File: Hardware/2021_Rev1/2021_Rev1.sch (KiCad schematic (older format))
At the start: 37 parts

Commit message: Schematic almost finished
Switches, Joystick connector, Analog gauge
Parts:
- added Conn1: Joystick_OUT, symbol MRDT_Connectors:Molex_SL_04
- added Conn2: Joystick_GND, symbol MRDT_Connectors:Molex_SL_04
- added Conn3: ELEV, symbol MRDT_Connectors:Molex_SL_02
- added Conn4: AZI, symbol MRDT_Connectors:Molex_SL_02
- added Conn5: Switches, symbol MRDT_Connectors:Molex_SL_10
- added Conn6: Green_LED, symbol MRDT_Connectors:Molex_SL_02
- added J?: Conn_01x18_Shielded, symbol Connector_Generic_Shielded:Conn_01x18_Shielded
- U2: renamed from U?; value LM2576D2TR4 -> LM2576SX-3.3
- U3: renamed from U?; value LM2576D2TR4 -> LM2576SX-5.0
- gave numbers to parts that had none: 28
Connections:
- wire segments 134 -> 237
- no-connect marks 5 -> 71

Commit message: Schematic almost finished
added LCD display
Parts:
- removed J?: Conn_01x18_Shielded, symbol Connector_Generic_Shielded:Conn_01x18_Shielded
- added 4.7K (x2): R, symbol Device:R
- added U?: PCF8574, symbol Interface_Expansion:PCF8574
- added U?: RC1602A, Display:RC1602A, symbol Display_Character:RC1602A
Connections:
- net labels added: P3, SCL, SDA, VO, k
- wire segments 237 -> 283
- no-connect marks 71 -> 76
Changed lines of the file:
@@
 U 1 1 5FABE786
 P 7000 4500
-F 0 "Conn6" H 7128 4658 60  0000 L CNN
-F 1 "Green_LED" H 7128 4552 60  0000 L CNN
+F 0 "Conn6" H 6900 4350 60  0000 L CNN
+F 1 "Green_LED" H 6850 4450 60  0000 L CNN
 F 2 "" H 7000 4400 60  0001 C CNN
 F 3 "" H 7000 4400 60  0001 C CNN
@@
 	5350 4400 5150 4400
 $Comp
-L Connector_Generic_Shielded:Conn_01x18_Shielded J?
-U 1 1 60174413
-P 10300 3750
-F 0 "J?" H 10388 3663 50  0000 L CNN
-F 1 "Conn_01x18_Shielded" H 10388 3572 50  0000 L CNN
-F 2 "" H 10300 3750 50  0001 C CNN
-F 3 "~" H 10300 3750 50  0001 C CNN
-	1    10300 3750
-	1    0    0    -1
-$EndComp
+L Display_Character:RC1602A U?
+U 1 1 5FA70A2A
+P 9650 5500
+F 0 "U?" H 9800 6300 50  0000 C CNN
+F 1 "RC1602A" H 9900 6200 50  0000 C CNN
+F 2 "Display:RC1602A" H 9750 4700 50  0001 C CNN
+F 3 "http://www.raystar-optronics.com/down.php?ProID=18" H 9750 5400 50  0001 C CNN
+	1    9650 5500
+	1    0    0    -1
+$EndComp
+Wire Wire Line
+	8950 5000 9250 5000
+Wire Wire Line
+	8950 5100 9250 5100
+Wire Wire Line
+	8950 5200 9250 5200
+Wire Wire Line
+	8950 5700 9000 5700
+Wire Wire Line
+	9000 5700 9000 6000
+Wire Wire Line
+	9000 6000 9250 6000
+Wire Wire Line
+	8950 5600 9050 5600
+Wire Wire Line
+	9050 5600 9050 5900
+Wire Wire Line
+	9050 5900 9250 5900
+Wire Wire Line
+	8950 5500 9100 5500
+Wire Wire Line
+	9100 5500 9100 5800
+Wire Wire Line
+	9100 5800 9250 5800
+Wire Wire Line
+	8950 5400 9150 5400
+Wire Wire Line
+	9150 5400 9150 5700
+Wire Wire Line
+	9150 5700 9250 5700
+NoConn ~ 9200 5300
+NoConn ~ 9200 5400
+NoConn ~ 9200 5500
+NoConn ~ 9200 5600
+Wire Wire Line
+	9200 5300 9250 5300
+Wire Wire Line
+	9200 5400 9250 5400
+Wire Wire Line
+	9200 5500 9250 5500
+Wire Wire Line
+	9200 5600 9250 5600
+$Comp
+L power:GND #PWR?
+U 1 1 5FBB576D
+P 9650 6300
+F 0 "#PWR?" H 9650 6050 50  0001 C CNN
+F 1 "GND" H 9655 6127 50  0000 C CNN
+F 2 "" H 9650 6300 50  0001 C CNN
+F 3 "" H 9650 6300 50  0001 C CNN
+	1    9650 6300
+	1    0    0    -1
+$EndComp
+$Comp
+L power:GND #PWR?
+U 1 1 5FBB5B62
+P 8450 6200
+F 0 "#PWR?" H 8450 5950 50  0001 C CNN
+F 1 "GND" H 8455 6027 50  0000 C CNN
+F 2 "" H 8450 6200 50  0001 C CNN
+F 3 "" H 8450 6200 50  0001 C CNN
+	1    8450 6200
+	1    0    0    -1
+$EndComp
+$Comp
+L power:GND #PWR?
+U 1 1 5FBB69D1
+P 7750 5900
+F 0 "#PWR?" H 7750 5650 50  0001 C CNN
+F 1 "GND" H 7755 5727 50  0000 C CNN
+F 2 "" H 7750 5900 50  0001 C CNN
+F 3 "" H 7750 5900 50  0001 C CNN
+	1    7750 5900
+	1    0    0    -1
+$EndComp
+NoConn ~ 7850 5800
+Wire Wire Line
+	8450 6100 8450 6200
+Wire Wire Line
+	9650 6200 9650 6300
+Wire Wire Line
+	7850 5800 7950 5800
+Wire Wire Line
+	7750 5900 7750 5500
+Wire Wire Line
+	7750 5300 7950 5300
+Wire Wire Line
+	7950 5400 7750 5400
+Connection ~ 7750 5400
+Wire Wire Line
+	7750 5400 7750 5300
+Wire Wire Line
+	7950 5500 7750 5500
+Connection ~ 7750 5500
+Wire Wire Line
+	7750 5500 7750 5400
+Text GLabel 9000 5300 2    50   Output ~ 0
+P3
+Wire Wire Line
+	8950 5300 9000 5300
+Text GLabel 10150 5300 2    50   Output ~ 0
+VO
+$Comp
+L power:+5V #PWR?
+U 1 1 5FC8AC31
+P 10600 5800
+F 0 "#PWR?" H 10600 5650 50  0001 C CNN
+F 1 "+5V" H 10615 5973 50  0000 C CNN
+F 2 "" H 10600 5800 50  0001 C CNN
+F 3 "" H 10600 5800 50  0001 C CNN
+	1    10600 5800
+	1    0    0    -1
+$EndComp
+Text GLabel 10150 5700 2    50   Output ~ 0
+k
+Text GLabel 7550 5000 0    50   Output ~ 0
+SCL
+Text GLabel 7550 5100 0    50   Output ~ 0
+SDA
+$Comp
+L power:+5V #PWR?
+U 1 1 5FC8EC9F
+P 7450 4600
+F 0 "#PWR?" H 7450 4450 50  0001 C CNN
+F 1 "+5V" H 7465 4773 50  0000 C CNN
+F 2 "" H 7450 4600 50  0001 C CNN
+F 3 "" H 7450 4600 50  0001 C CNN
+	1    7450 4600
+	1    0    0    -1
+$EndComp
+$Comp
+L Device:R 4.7K
+U 1 1 5FCAFDA1
+P 7650 4800
+F 0 "4.7K" V 7650 4700 50  0000 L CNN
+F 1 "R" H 7720 4755 50  0000 L CNN
+F 2 "" V 7580 4800 50  0001 C CNN
+F 3 "~" H 7650 4800 50  0001 C CNN
+	1    7650 4800
+	1    0    0    -1
+$EndComp
+$Comp
+L Device:R 4.7K
+U 1 1 5FCB0E54
+P 7850 4800
+F 0 "4.7K" V 7850 4700 50  0000 L CNN
+F 1 "R" H 7920 4755 50  0000 L CNN
+F 2 "" V 7780 4800 50  0001 C CNN
+F 3 "~" H 7850 4800 50  0001 C CNN
+	1    7850 4800
+	1    0    0    -1
+$EndComp
+$Comp
+L Interface_Expansion:PCF8574 U?
+U 1 1 5FA6EB0D
+P 8450 5400
+F 0 "U?" H 8600 6200 50  0000 C CNN
+F 1 "PCF8574" H 8700 6100 50  0000 C CNN
+F 2 "" H 8450 5400 50  0001 C CNN
+F 3 "http://www.nxp.com/documents/data_sheet/PCF8574_PCF8574A.pdf" H 8450 5400 50  0001 C CNN
+	1    8450 5400
+	1    0    0    -1
+$EndComp
+Wire Wire Line
+	7550 5000 7850 5000
+Wire Wire Line
+	7550 5100 7650 5100
+Wire Wire Line
+	7650 4950 7650 5100
+Connection ~ 7650 5100
+Wire Wire Line
+	7650 5100 7950 5100
+Wire Wire Line
+	7850 4950 7850 5000
+Connection ~ 7850 5000
+Wire Wire Line
+	7850 5000 7950 5000
+Wire Wire Line
+	7450 4600 7650 4600
+Wire Wire Line
+	8450 4600 8450 4700
+Wire Wire Line
+	8450 4600 9650 4600
+Wire Wire Line
+	9650 4600 9650 4800
+Connection ~ 8450 4600
+Wire Wire Line
+	7850 4650 7850 4600
+Connection ~ 7850 4600
+Wire Wire Line
+	7850 4600 8450 4600
+Wire Wire Line
+	7650 4650 7650 4600
+Connection ~ 7650 4600
+Wire Wire Line
+	7650 4600 7850 4600
+Wire Wire Line
+	10050 5300 10150 5300
+Wire Wire Line
+	10050 5700 10150 5700
+Wire Wire Line
+	10050 5800 10600 5800
 $EndSCHEMATC

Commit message: Layout Started
Bucks and LCD circuit replaced with OKIs and spark fun LCD
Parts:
- removed 4.7K (x2): R, symbol Device:R
- removed D1, D3: D_Schottky, symbol Device:D_Schottky
- removed D2, D4: GREEN, symbol Device:LED
- removed L1, L2: 100uH, symbol Device:L_Small
- removed R1: 330, symbol Device:R
- removed R2: 500, symbol Device:R
- removed TP1, TP2: TestPoint, symbol Connector:TestPoint
- removed U2: LM2576SX-3.3, symbol MRDT_Devices:LM2576D2TR4
- removed U3: LM2576SX-5.0, symbol MRDT_Devices:LM2576D2TR4
- removed U?: PCF8574, symbol Interface_Expansion:PCF8574
- removed U?: RC1602A, Display:RC1602A, symbol Display_Character:RC1602A
- added BT1: BC9VPC, Packages:BAT_BC9VPC, symbol BC9VPC:BC9VPC
- added Conn8: Molex_SL_03, MRDT_Connectors:MOLEX_SL_03_Vertical, symbol MRDT_Connectors:Molex_SL_03
- added U2, U3: OKI, MRDT_Devices:OKI_Horizontal, symbol MRDT_Devices:OKI
- C1, C3: value 100uF -> 10uF; footprint (none) -> Capacitor_SMD:C_0603_1608Metric_Pad1.08x0.95mm_HandSolder
- C2, C4: value 1000uF -> 10uF; footprint (none) -> Capacitor_SMD:C_0603_1608Metric_Pad1.08x0.95mm_HandSolder
- C5, C6, C7: footprint (none) -> Capacitor_SMD:C_0603_1608Metric_Pad1.08x0.95mm_HandSolder
- Conn2: renamed from Conn1; footprint (none) -> MRDT_Connectors:MOLEX_SL_04_Vertical
- Conn3: renamed from Conn2; footprint (none) -> MRDT_Connectors:MOLEX_SL_04_Vertical
- Conn4: renamed from Conn3; footprint (none) -> MRDT_Connectors:MOLEX_SL_02_Vertical
- Conn5: renamed from Conn4; footprint (none) -> MRDT_Connectors:MOLEX_SL_02_Vertical
- Conn6: renamed from Conn5; footprint (none) -> MRDT_Connectors:MOLEX_SL_10_Vertical
- Conn7: renamed from Conn6; footprint (none) -> MRDT_Connectors:MOLEX_SL_02_Vertical
- D1: renamed from D5; footprint (none) -> LED_SMD:LED_0603_1608Metric_Pad1.05x0.95mm_HandSolder
- D2: renamed from D6; footprint (none) -> LED_SMD:LED_0603_1608Metric_Pad1.05x0.95mm_HandSolder
- J1: footprint (none) -> Connector_USB:USB_A_Stewart_SS-52100-001_Horizontal
- R1: renamed from R3; footprint (none) -> Resistor_SMD:R_0603_1608Metric_Pad0.98x0.95mm_HandSolder
- R2: renamed from R4; footprint (none) -> Resistor_SMD:R_0603_1608Metric_Pad0.98x0.95mm_HandSolder
- R3: renamed from R5; footprint (none) -> Resistor_SMD:R_0603_1608Metric_Pad0.98x0.95mm_HandSolder
- R4: renamed from R6; footprint (none) -> Resistor_SMD:R_0603_1608Metric_Pad0.98x0.95mm_HandSolder
- R5: renamed from R7; footprint (none) -> Resistor_SMD:R_0603_1608Metric_Pad0.98x0.95mm_HandSolder
- R6: renamed from R8; footprint (none) -> Resistor_SMD:R_0603_1608Metric_Pad0.98x0.95mm_HandSolder
- U1: footprint (none) -> MRDT_Shields:TM4C129E_Launchpad_FULL_THT_TOP
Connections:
- net labels added: +3.3V, LCD_TX
- net labels removed: P3, SCL, SDA, VO, k
- wire segments 283 -> 204
- no-connect marks 76 -> 70

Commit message: resistor values added to CTL pins
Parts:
- added R? (x2): 330, symbol Device:R_Small
- BT1: symbol BC9VPC:BC9VPC -> 2021_Rev1-rescue:BC9VPC-BC9VPC
- J1: symbol Connector:USB_A -> 2021_Rev1-rescue:USB_A-Connector
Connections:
- net AZI_CTL: now also R?.2; no longer Conn5.1
- net ELEV_CTL: now also R?.2; no longer Conn4.1
- new net: Conn4.1, R?.1
- new net: Conn5.1, R?.1
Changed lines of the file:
@@
 EESchema Schematic File Version 4
+LIBS:2021_Rev1-cache
 EELAYER 30 0
 EELAYER END
@@
 	900  2800 1050 2800
 $Comp
-L Connector:USB_A J1
+L 2021_Rev1-rescue:USB_A-Connector J1
 U 1 1 5FA36A0D
 P 5800 1600
@@
 Wire Wire Line
 	2050 2500 1950 2500
-Text GLabel 5200 3900 0    39   Input ~ 0
+Text GLabel 4970 3900 0    39   Input ~ 0
 ELEV_CTL
 Wire Wire Line
@@
 Wire Wire Line
 	5350 4000 5200 4000
-Text GLabel 5150 4400 0    39   Input ~ 0
+Text GLabel 4960 4400 0    39   Input ~ 0
 AZI_CTL
 $Comp
@@
 Wire Wire Line
 	5350 4500 5200 4500
-Wire Wire Line
-	5350 4400 5150 4400
 $Comp
 L power:+5V #PWR022
@@
 	1750 4900 2250 4900
 $Comp
-L BC9VPC:BC9VPC BT1
+L 2021_Rev1-rescue:BC9VPC-BC9VPC BT1
 U 1 1 5FE356D0
 P 2800 5800
@@
 Wire Wire Line
 	2800 6100 2800 6300
+$Comp
+L Device:R_Small R?
+U 1 1 5FBB25F6
+P 5100 3900
+F 0 "R?" V 5020 3900 50  0000 C CNN
+F 1 "330" V 5100 3900 50  0000 C CNN
+F 2 "" H 5100 3900 50  0001 C CNN
+F 3 "~" H 5100 3900 50  0001 C CNN
+	1    5100 3900
+	0    1    1    0
+$EndComp
+$Comp
+L Device:R_Small R?
+U 1 1 5FBB3DCB
+P 5090 4400
+F 0 "R?" V 5010 4400 50  0000 C CNN
+F 1 "330" V 5090 4400 50  0000 C CNN
+F 2 "" H 5090 4400 50  0001 C CNN
+F 3 "~" H 5090 4400 50  0001 C CNN
+	1    5090 4400
+	0    1    1    0
+$EndComp
+Wire Wire Line
+	5000 3900 4970 3900
+Wire Wire Line
+	4990 4400 4960 4400
+Wire Wire Line
+	5350 4400 5190 4400
 $EndSCHEMATC

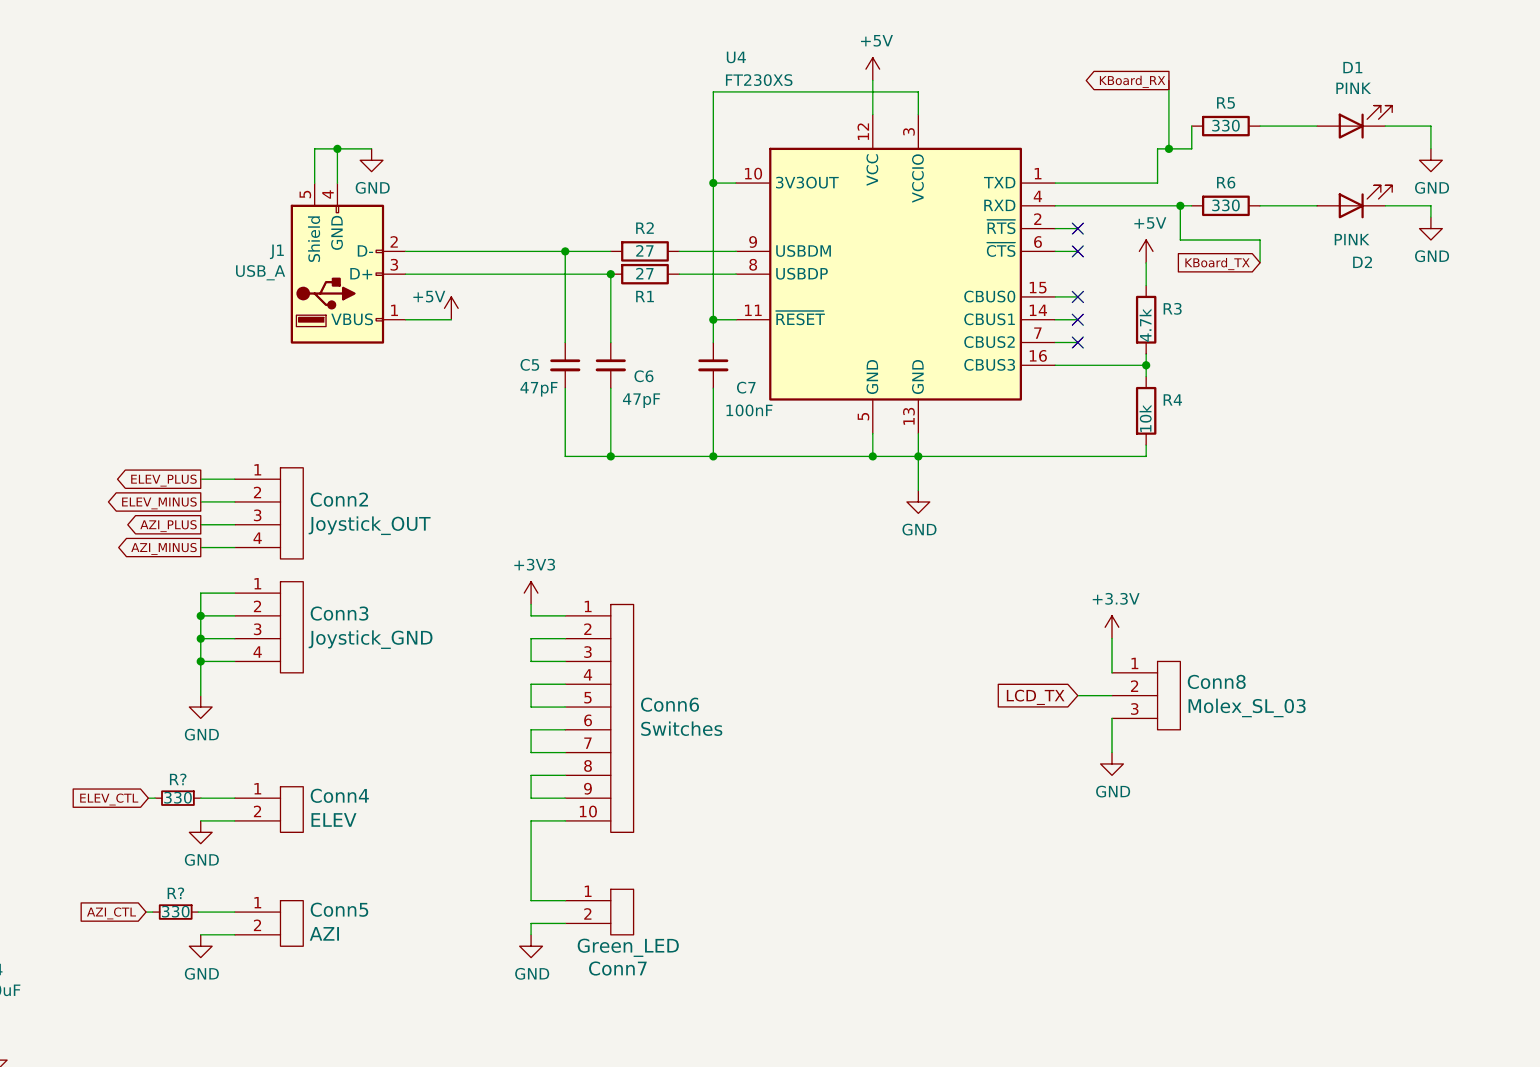
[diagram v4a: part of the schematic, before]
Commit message: Updated Schematic and Layout
Changed joystick pins from GND to 3.3V and updated USB circuit to a known working circuit
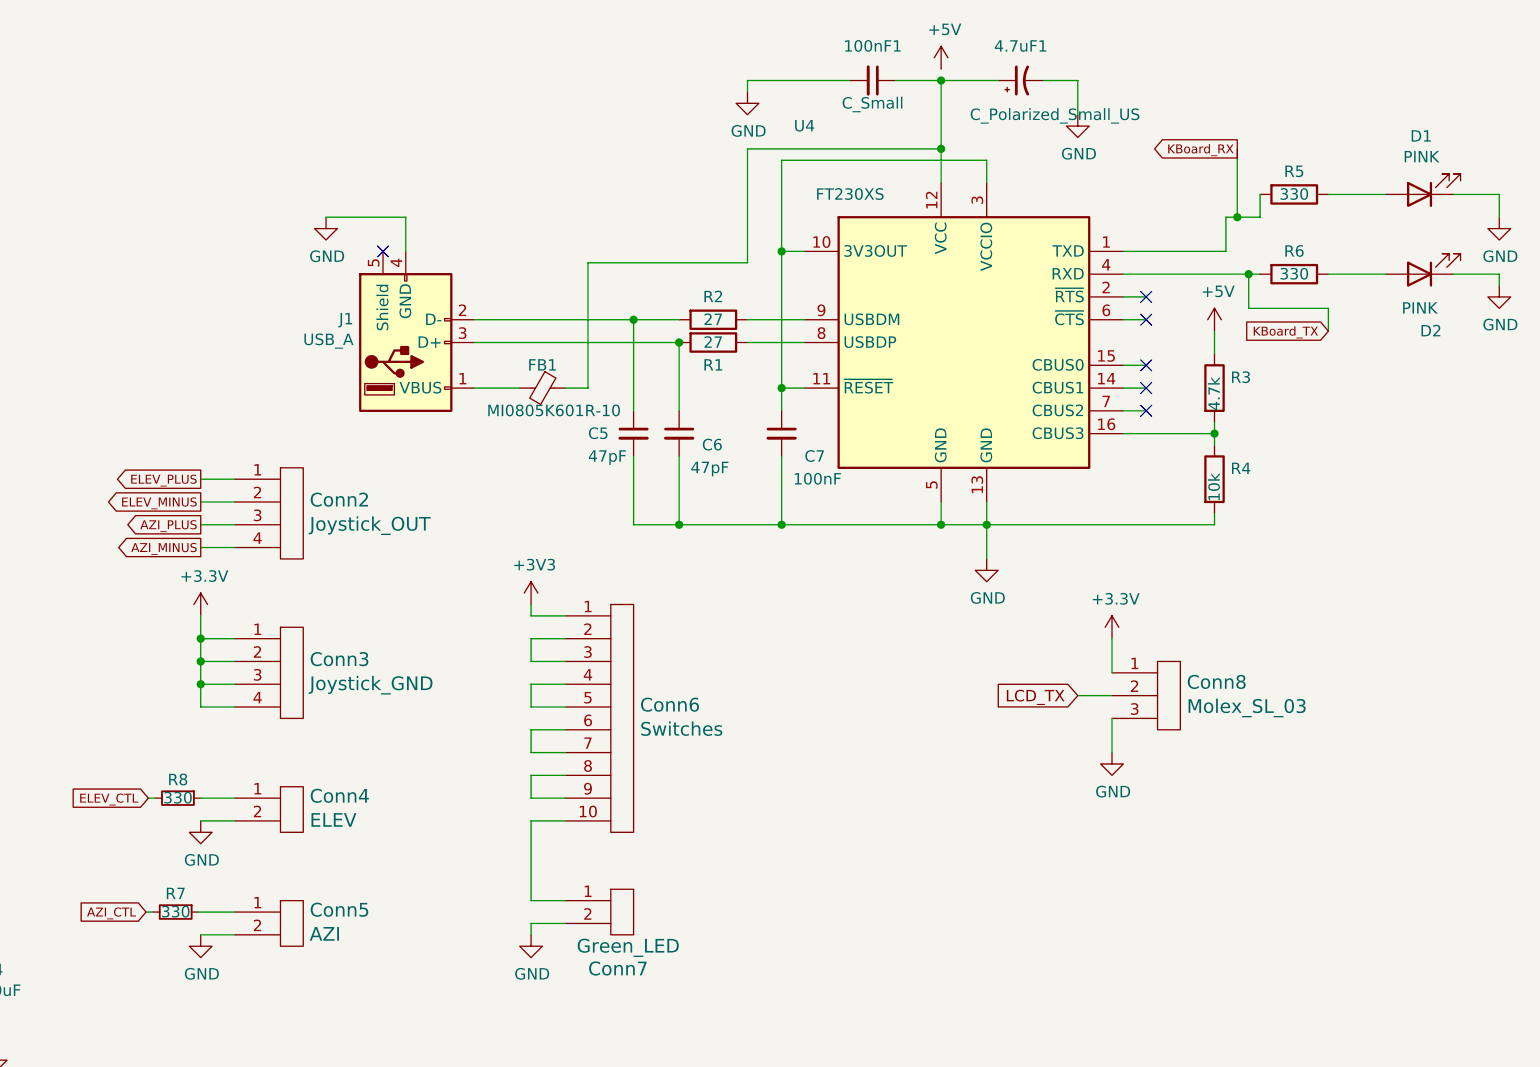
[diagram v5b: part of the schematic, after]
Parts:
- added 100nF1: C_Small, Capacitor_SMD:C_0603_1608Metric_Pad1.08x0.95mm_HandSolder, symbol Device:C_Small
- added 4.7uF1: C_Polarized_Small_US, Capacitor_THT:CP_Radial_D5.0mm_P2.50mm, symbol Device:C_Polarized_Small_US
- added FB1: MI0805K601R-10, Resistor_SMD:R_0805_2012Metric_Pad1.20x1.40mm_HandSolder, symbol Device:FerriteBead_Small
- R7, R8: renamed from R?; footprint (none) -> Resistor_SMD:R_0603_1608Metric_Pad0.98x0.95mm_HandSolder
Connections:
- net +3V3: now also Conn3.1, Conn3.2, Conn3.3, Conn3.4
- net +5V: no longer J1.1 (VBUS), U4.12 (VCC)
- net GND: now also 100nF1.2, 4.7uF1.2; no longer Conn3.1, Conn3.2, Conn3.3, Conn3.4, J1.5 (Shield)
- new net: 100nF1.1, 4.7uF1.1, FB1.1, U4.12 (VCC)
- new net: FB1.2, J1.1 (VBUS)
- no-connect marks 70 -> 71
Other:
- moved on the sheet: C5, C6, C7, Conn3, D1, D2, J1, R1, R2, R3, R4, R5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
